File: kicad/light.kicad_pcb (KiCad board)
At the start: 2 copper layers, 58 x 40 mm, 139 parts, among them J2 USB_C_Receptacle_USB2.0_16P, J3 Barrell Jack, J4 01x04, J5 SM03B-SRSS-TB, J6 SM03B-SRSS-TB, J9 Conn_01x09_MountingPin, Q1 NMOS, Q2 NMOS, Q3 NMOS, SW1 Boot, SW3 On/Off, SW4 Mode, U1 RP2350A-QFN60, U10 MAX6816, U2 TPS5405DR, U3 W25Q128JVS, U4 LBEE5KL1YN-814, U5 TPS2115ADRBR, U6 TPS2115ADRBR, U7 HDC1080, U8 MAX6816, U9 MAX6816, Y1 ABM8-272-T3

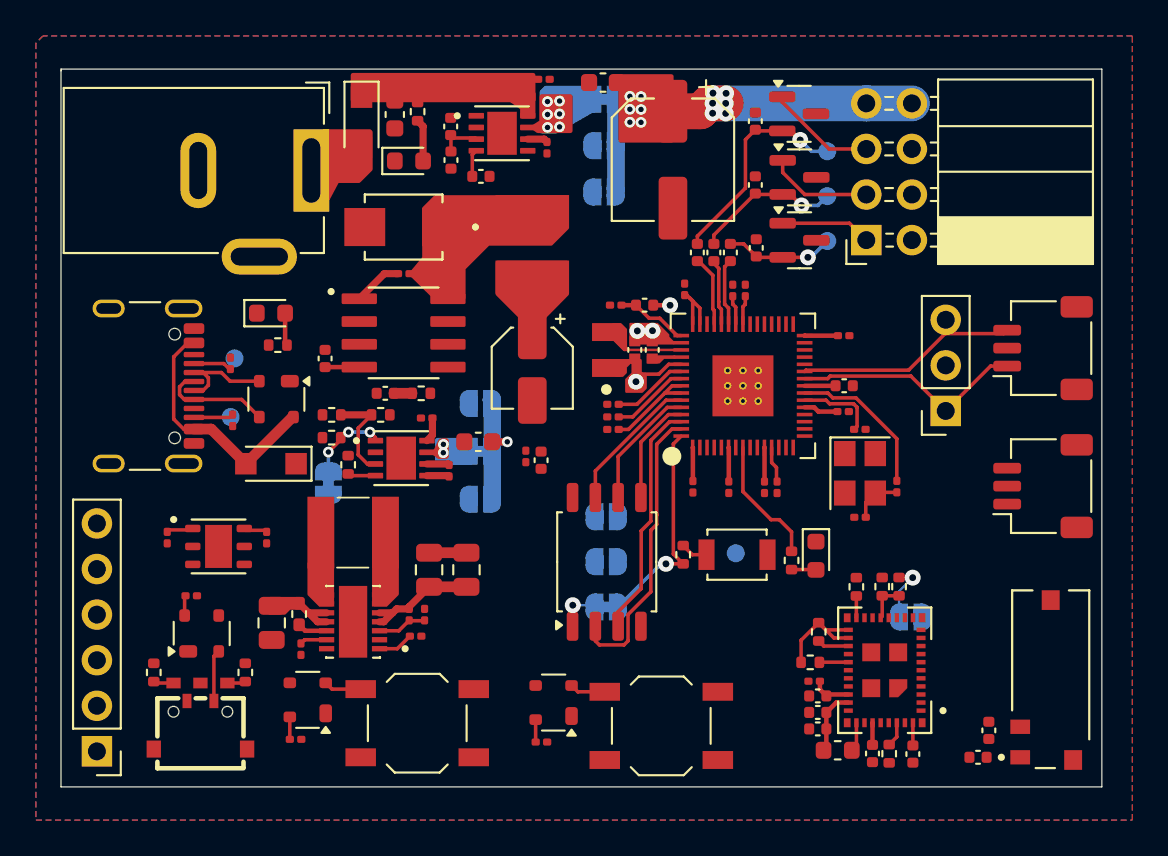
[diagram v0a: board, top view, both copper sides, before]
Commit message: route wireless module
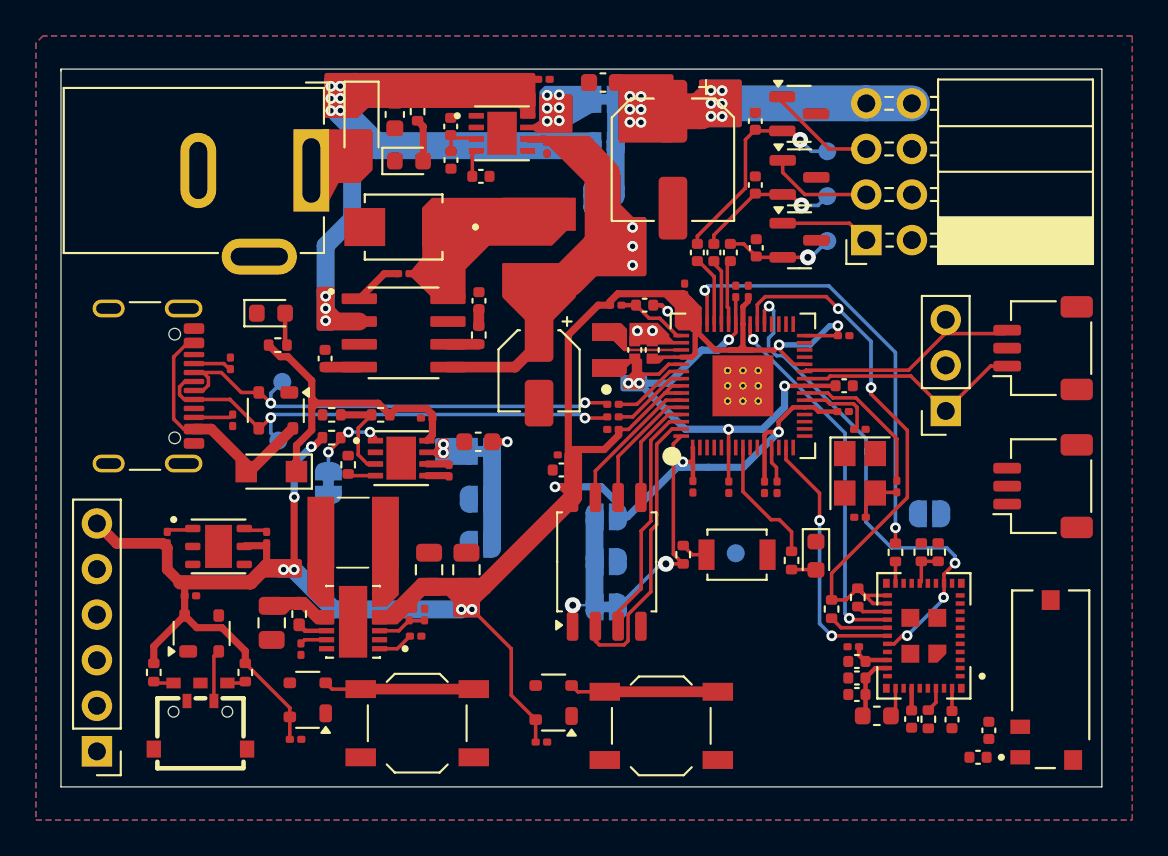
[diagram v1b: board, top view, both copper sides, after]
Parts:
- moved JP13 7.85 mm to (148.9, 104.0)
- moved C26 7.34 mm to (148.8, 90.4), turned to 90 degrees
- moved JP1 5.85 mm to (173.9, 102.3), turned to 180 degrees
- moved R17 4.57 mm to (148.8, 92.3), turned to 90 degrees
- moved R19 3.20 mm to (168.4, 107.6), turned to 90 degrees
- moved TP2 2.97 mm to (137.6, 98.2)
- moved TP3 2.97 mm to (137.8, 94.9)
- moved C16 2.90 mm to (169.9, 110.5)
- moved C17 2.90 mm to (169.7, 109.7)
- moved C28 2.90 mm to (169.9, 111.4)
- moved C29 2.90 mm to (172.9, 113.7)
- moved C30 2.90 mm to (169.9, 112.3)
- moved C45 2.90 mm to (175.2, 113.7)
- moved L4 2.90 mm to (171.0, 113.5)
- moved R18 2.90 mm to (169.9, 106.9)
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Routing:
- net +3V3: track 31.7 -> 150.2 mm, vias 0 -> 11
- net /WL_ON: track 0.00 -> 28.7 mm, vias 0 -> 4
- net +12V: track 0.00 -> 25.0 mm, vias 0 -> 9
- net /WL_CLK: track 0.00 -> 24.9 mm, vias 0 -> 2
- net /WL_D: track 6.44 -> 31.2 mm, vias 0 -> 2
- net /USB_D-: track 6.10 -> 27.6 mm, vias 0 -> 2
- net /USB_D+: track 6.32 -> 27.9 mm, vias 0 -> 2
- net /WL_CS: track 0.00 -> 20.8 mm, vias 0 -> 2
- net /VREG5: track 2.39 -> 22.4 mm, vias 0 -> 3
- net +1V1: track 8.00 -> 27.9 mm, vias 1 -> 5
- net /VBUS: track 1.39 -> 18.0 mm
- net /WL_HOST_WAKE: track 0.00 -> 14.7 mm, vias 0 -> 2
- net Net-(U9-IN): track 1.99 -> 8.29 mm
- net Net-(U10-IN): track 2.09 -> 8.39 mm
- net Net-(JP1-A): track 3.27 -> 0.00 mm, vias 1 -> 0
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
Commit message: finish routing
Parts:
- removed JP1: VBUS, Jumper:SolderJumper-2_P1.3mm_Open_RoundedPad1.0x1.5mm
- removed JP2: PWR_STAT, Jumper:SolderJumper-2_P1.3mm_Bridged_RoundedPad1.0x1.5mm
- removed R20: 10K, Resistor_SMD:R_0402_1005Metric
- removed R21: 5.6K, Resistor_SMD:R_0402_1005Metric
- removed R23: 100K, Resistor_SMD:R_0402_1005Metric
- moved R4 10.6 mm to (166.0, 90.2), turned to 0 degrees
- moved D73 6.95 mm to (165.8, 111.3), turned to 90 degrees
- moved R44 3.79 mm to (165.8, 108.6)
- moved TP1 3.57 mm to (160.5, 106.9)
- moved C40 3.01 mm to (150.7, 112.4), turned to -90 degrees
- moved C41 2.82 mm to (137.0, 112.5), turned to -90 degrees
- moved R8 2.14 mm to (172.5, 98.7)
- moved C34 1.04 mm to (149.5, 98.9), turned to -90 degrees
- moved C11 0.91 mm to (165.4, 100.1), turned to 0 degrees
- moved U9 0.81 mm to (152.9, 112.0)
- moved C32 0.65 mm to (146.5, 97.0), turned to 0 degrees
- moved C17 0.39 mm to (170.1, 109.6), turned to 0 degrees
- moved R13 0.32 mm to (139.2, 109.7)
- moved U10 0.26 mm to (139.2, 112.4)
- moved C33 0.18 mm to (147.0, 99.8)
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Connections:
- J9 pad 1: /GPIO0 -> /GPIO2
- J9 pad 3: /GPIO2 -> /GPIO0
- R4 pad 1: Net-(U1-GPIO8) -> Net-(U1-GPIO20)
- U1 pad 10: unconnected-(U1-GPIO7-Pad10) -> /WE_SCL
- U1 pad 12: Net-(U1-GPIO8) -> unconnected-(U1-GPIO8-Pad12)
- U1 pad 15: /PWR_STAT -> unconnected-(U1-GPIO11-Pad15)
- U1 pad 32: /WE_SDA -> Net-(U1-GPIO20)
- U1 pad 33: /WE_SCL -> unconnected-(U1-GPIO21-Pad33)
- U1 pad 9: unconnected-(U1-GPIO6-Pad9) -> /WE_SDA
- U4 pad 17: /WL_GPIO2 -> unconnected-(U4-WL_GPIO_2-Pad17)
- U5 pad 1: Net-(JP2-A) -> unconnected-(U5-STAT-Pad1)
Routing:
- net /GPIO0: track 0.00 -> 77.9 mm, vias 0 -> 4
- net /GPIO1: track 0.00 -> 69.7 mm, vias 0 -> 2
- net /BTN_MODE: track 0.00 -> 69.6 mm, vias 0 -> 4
- net /WE_SDA: track 1.50 -> 61.8 mm, vias 0 -> 4
- net /BTN_ON_OFF: track 0.00 -> 59.7 mm, vias 0 -> 2
- net /GPIO2: track 0.00 -> 54.9 mm
- net /ROT_ENC_B: track 1.13 -> 54.6 mm, vias 0 -> 2
- net /ROT_ENC_A: track 1.03 -> 48.5 mm, vias 0 -> 2
- net /ROT_ENC_SW: track 0.00 -> 42.8 mm, vias 0 -> 2
- net /WL_GPIO1: track 1.51 -> 43.2 mm, vias 0 -> 4
- net /WE_SCL: track 1.32 -> 38.0 mm, vias 0 -> 2
- net /PWR_DRGB_LVL: track 0.00 -> 36.4 mm, vias 0 -> 2
- net /VSYS: track 1.87 -> 33.6 mm, vias 1 -> 3
- net /ARGB-DATA: track 0.00 -> 13.1 mm
- net /VREG5: track 22.4 -> 30.7 mm, vias 3 -> 5
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- added copper zone on In1.Cu, net GND
- added copper zone on In2.Cu, net GND
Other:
- copper layers 2 -> 4

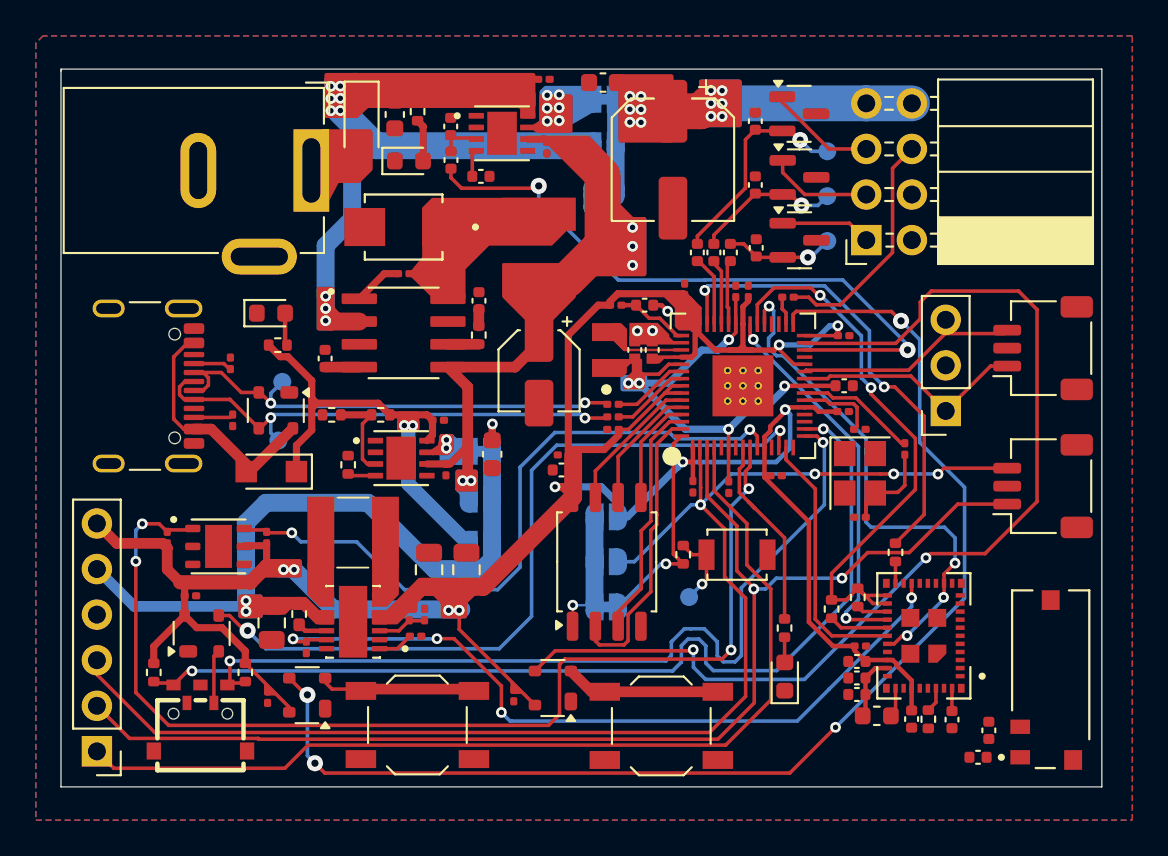
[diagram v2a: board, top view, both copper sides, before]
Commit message: tweak copper pour parameters; solve some DRC errors
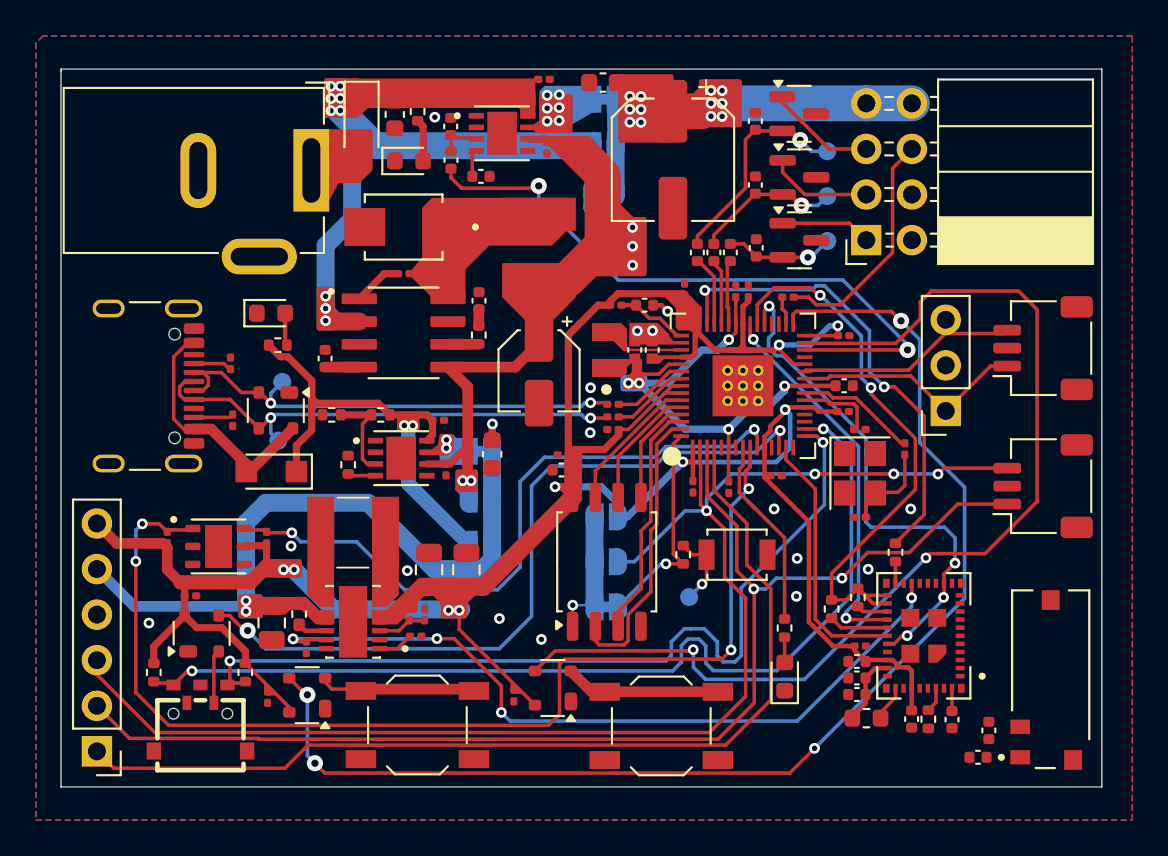
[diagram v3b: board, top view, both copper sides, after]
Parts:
- moved L4 0.59 mm to (170.4, 113.7)
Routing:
- net /WE_SCL: track 38.0 -> 37.4 mm
- net /ROT_ENC_SW: track 42.8 -> 42.3 mm
- net GND: vias 3 -> 16

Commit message: solve some DRC errors
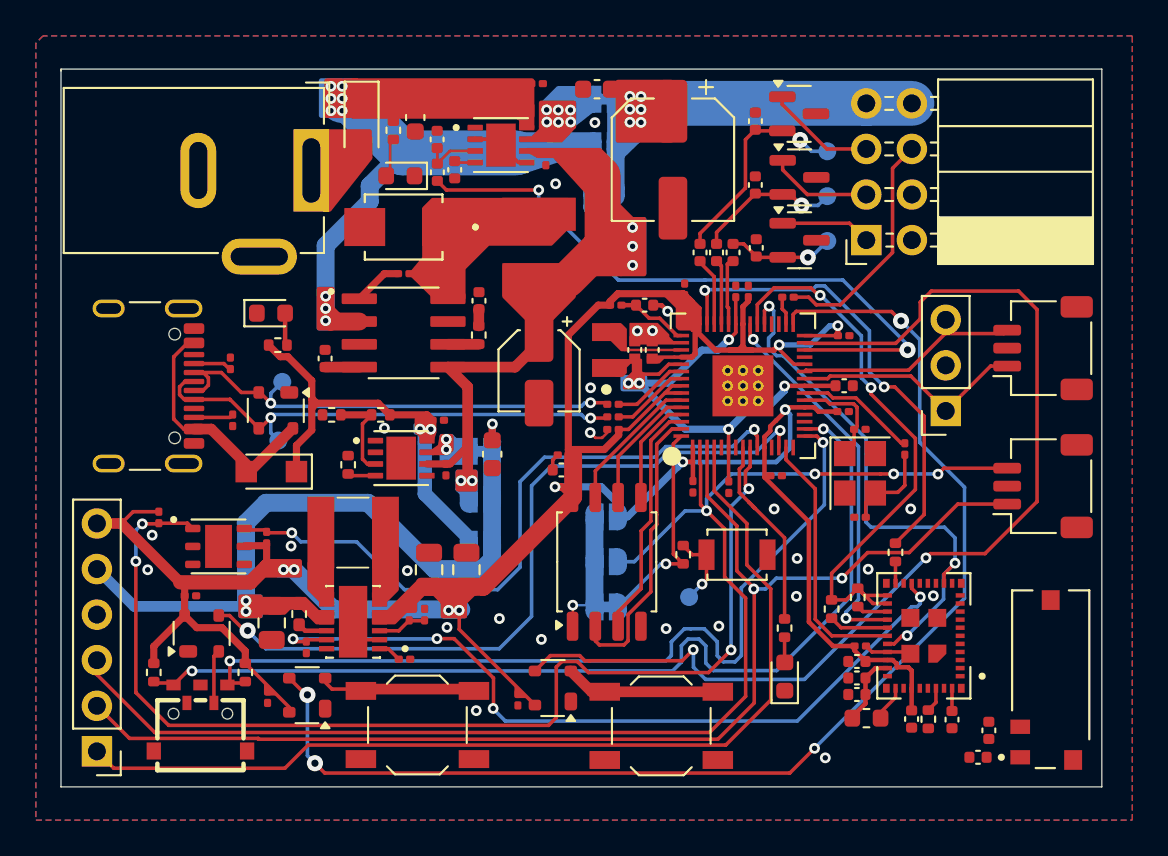
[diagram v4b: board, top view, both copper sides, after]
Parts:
- moved R5 1.70 mm to (144.0, 80.9)
- moved R35 1.50 mm to (147.4, 83.1), turned to -90 degrees
- moved C4 1.42 mm to (144.7, 110.4)
- moved R36 1.22 mm to (131.0, 102.5), turned to 90 degrees
- moved C24 1.15 mm to (145.2, 80.2)
- moved R34 1.04 mm to (146.5, 81.4)
- moved R33 1.02 mm to (146.5, 83.2)
- moved D68 0.96 mm to (144.4, 83.4), turned to 180 degrees
- moved C37 0.66 mm to (152.5, 82.5)
- moved U6 0.66 mm to (150.0, 81.7)
- moved C38 0.50 mm to (155.4, 78.6)
- moved C36 0.45 mm to (152.0, 78.3)
- moved C40 0.33 mm to (151.0, 112.6)
- moved R30 0.15 mm to (161.1, 87.7)
- moved R31 0.15 mm to (162.0, 87.7)
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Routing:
- net GND: track 0.94 -> 11.0 mm, vias 16 -> 25
- net /VREG5: track 30.7 -> 25.6 mm
- net /V_RGB: track 12.5 -> 15.8 mm, vias 12 -> 6
- net +12V: track 25.0 -> 22.3 mm
- net /VBUS: track 24.7 -> 23.0 mm
- net +3V3: track 155.4 -> 157.0 mm
- net /XIN: track 4.38 -> 5.95 mm
- net /WL_ON: track 29.3 -> 30.4 mm, vias 4 -> 3
- net Net-(U6-D1): track 2.44 -> 3.28 mm
- net /WL_GPIO1: track 43.2 -> 44.0 mm
- net Net-(VR1-VINA): track 1.98 -> 1.31 mm

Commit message: add mounting holes and fix isolated GND islands
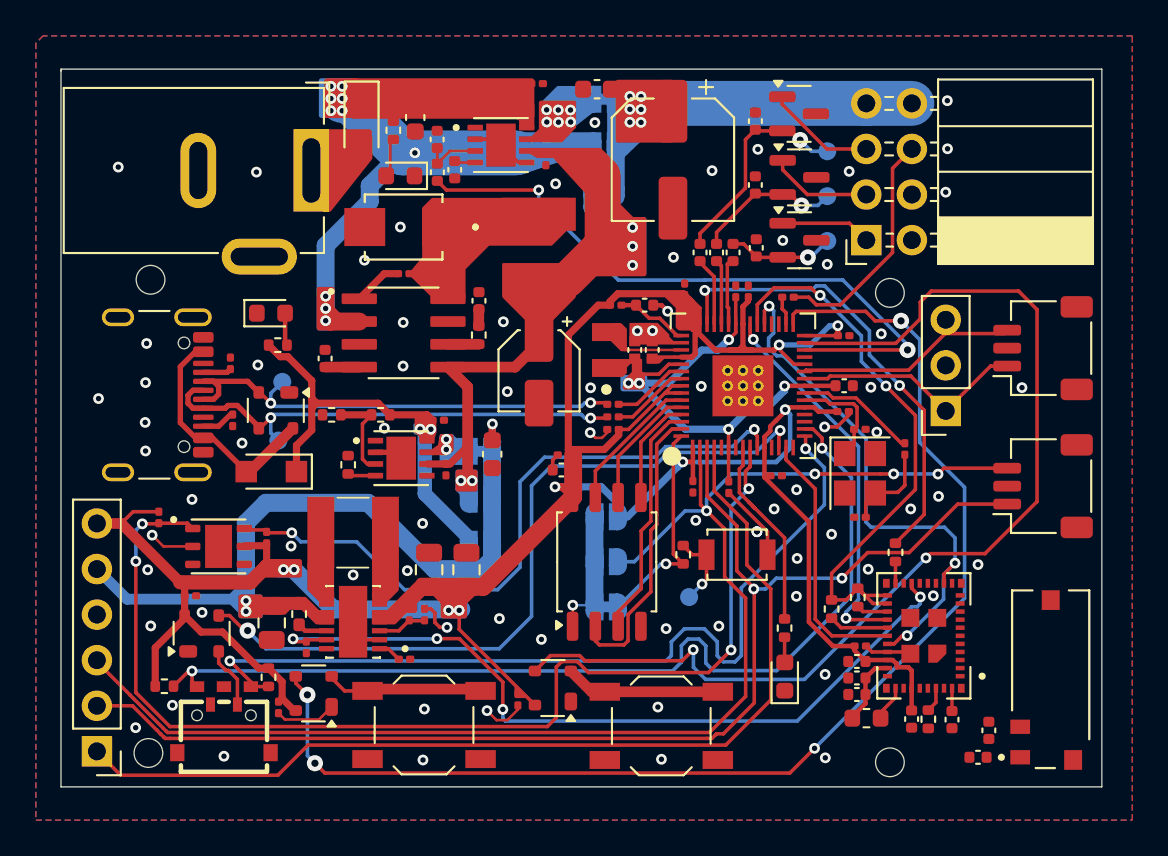
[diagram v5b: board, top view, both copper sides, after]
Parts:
- added ?: , , F.Cu at (171.7, 116.1)
- added ?: , , F.Cu at (130.4, 115.6)
- added ?: , , F.Cu at (130.5, 89.2)
- added REF**: 1.6mm hole, holes:1.6mm hole, F.Cu at (171.7, 90.0)
- moved R41 1.32 mm to (137.1, 111.4)
- moved R6 1.31 mm to (134.6, 113.7)
- moved R40 0.97 mm to (131.3, 111.9), turned to 0 degrees
- moved C41 0.83 mm to (137.6, 113.0)
- moved J2 0.71 mm to (129.8, 95.6)
- moved U10 0.37 mm to (139.6, 112.3)
- moved SW4 0.37 mm to (145.7, 114.0)
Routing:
- net GND: track 11.0 -> 29.1 mm, vias 25 -> 76
- net +3V3: track 157.0 -> 158.8 mm
- net Net-(U8-IN): track 2.87 -> 3.48 mm
- net /USB_D-: track 27.6 -> 27.0 mm
- net /ROT_ENC_B: track 54.6 -> 54.1 mm
- net Net-(J2-CC1): track 2.16 -> 1.58 mm
- net +12V: vias 9 -> 10
